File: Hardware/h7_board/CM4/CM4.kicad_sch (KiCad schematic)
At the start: 0 parts

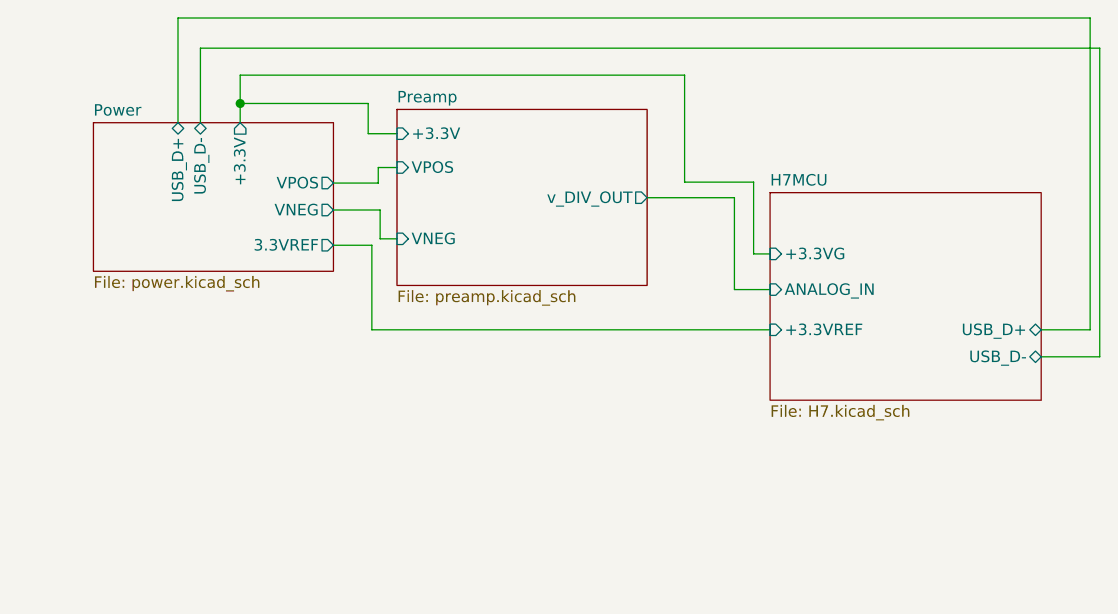
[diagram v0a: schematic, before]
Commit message: Edited Design to modify to LDO regulator and improve board layout
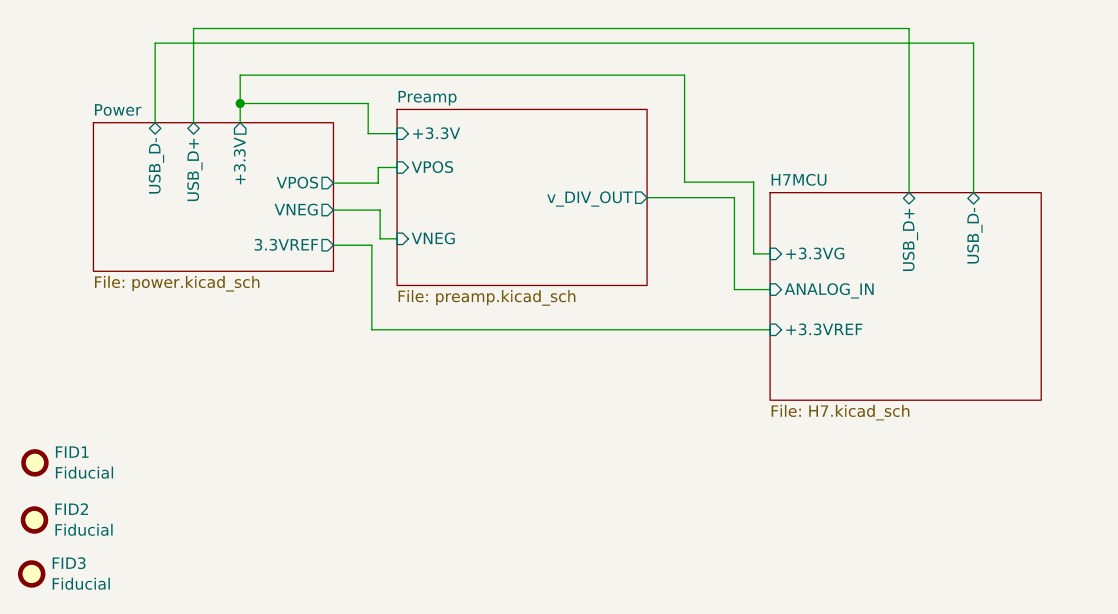
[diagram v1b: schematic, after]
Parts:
- added FID1, FID2, FID3: Fiducial, Fiducial:Fiducial_0.5mm_Mask1.5mm, symbol Mechanical:Fiducial
